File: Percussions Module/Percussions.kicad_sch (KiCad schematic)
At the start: 86 parts

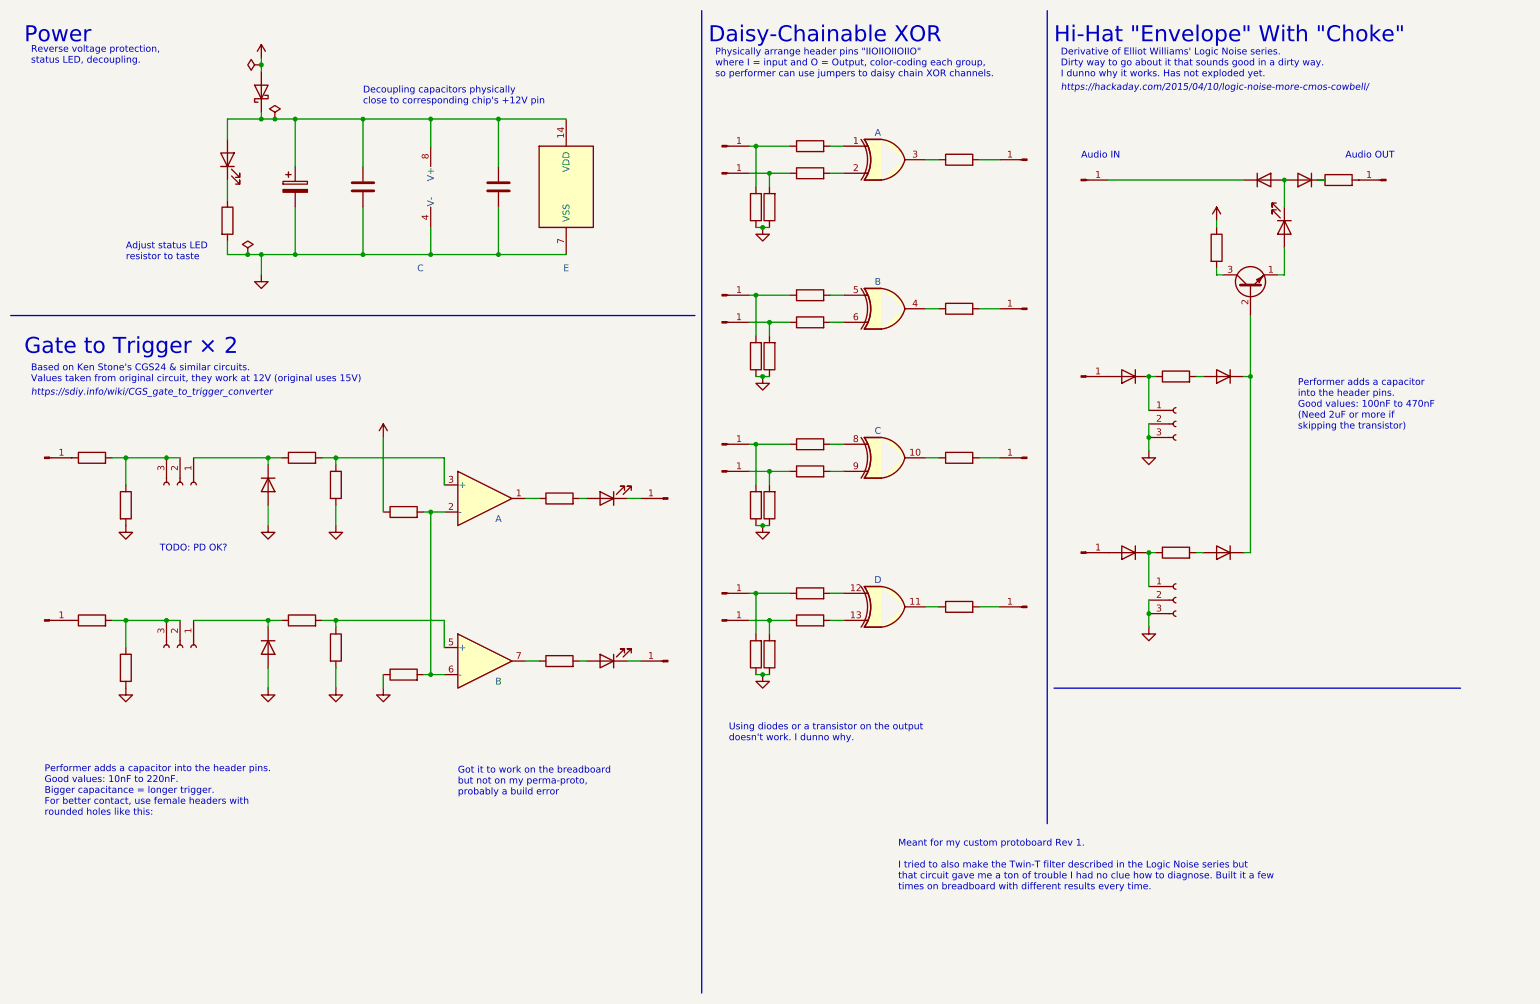
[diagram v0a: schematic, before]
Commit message: Try out switching sequencer
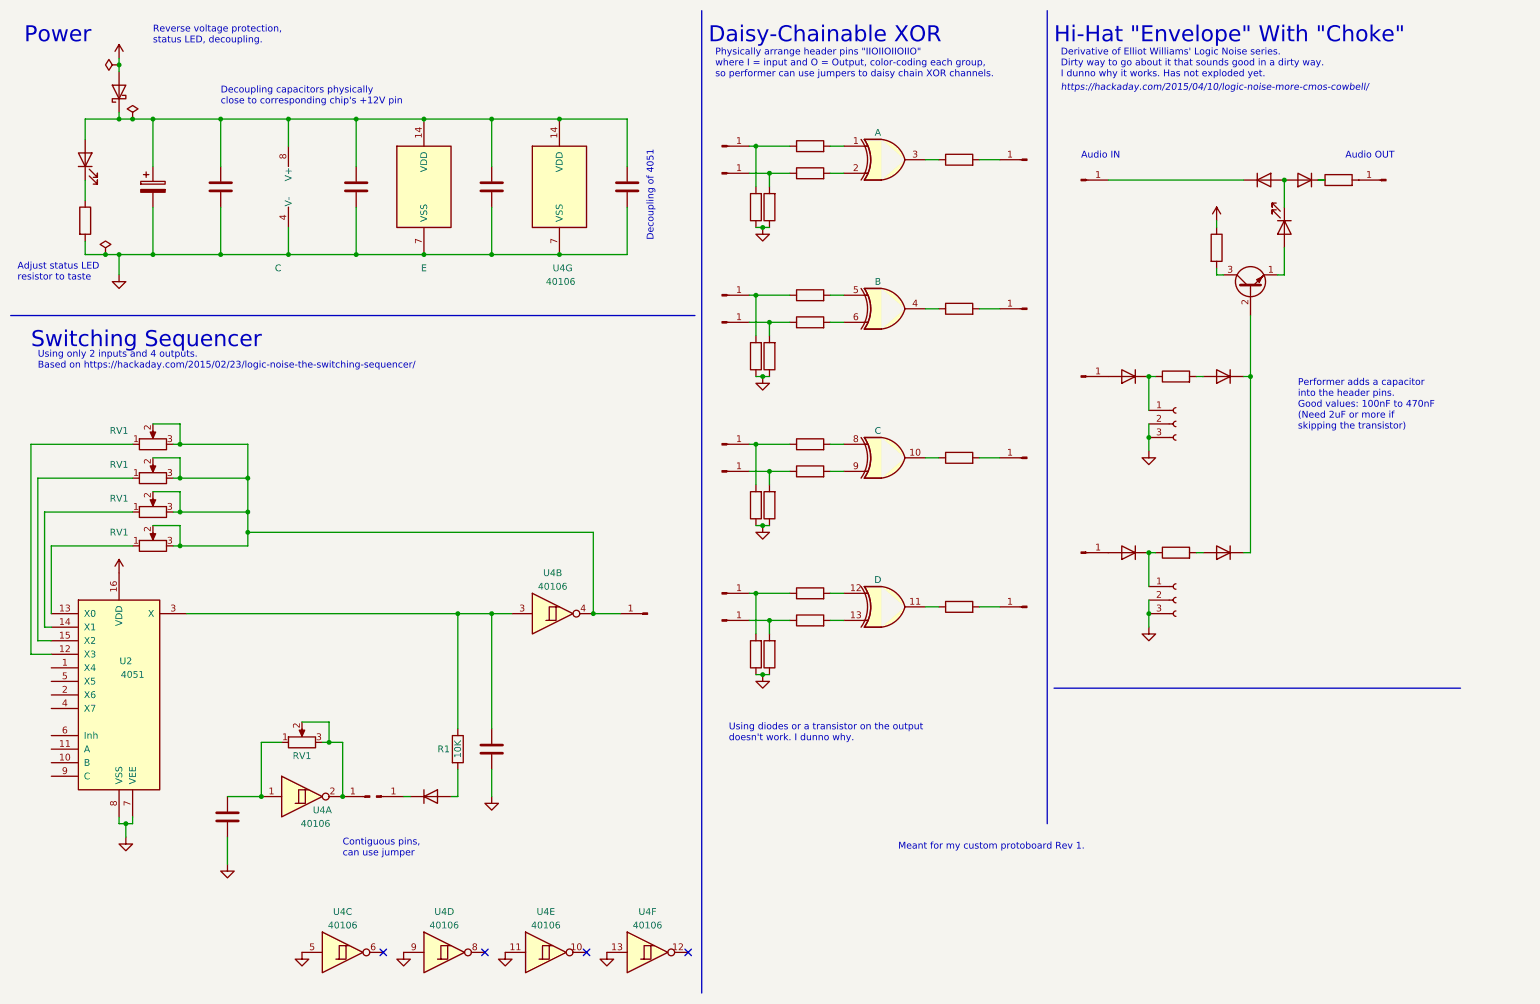
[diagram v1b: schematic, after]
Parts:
- removed ? (x4): (no value), symbol Connector:Conn_01x01_Male
- removed ? (x2): (no value), symbol Diode:1N4148
- removed ? (x12): (no value), symbol Device:R
- removed ? (x2): (no value), symbol Device:LED
- removed ? (x2): (no value), symbol Amplifier_Operational:LM358
- removed ? (x2): (no value), symbol Connector:Conn_01x03_Female
- added ? (x4): (no value), symbol Device:C
- added ?: (no value), symbol Diode:1N4148
- added ? (x3): (no value), symbol Connector:Conn_01x01_Male
- added R1: 10K, symbol Device:R
- added RV1 (x5): R_Potentiometer, symbol Device:R_Potentiometer
- added U2: 4051, symbol 4xxx:4051
- added U4: 40106, symbol 4xxx:40106
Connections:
- net +12V: now also U2.16 (VDD)
- net GND: now also ?.2, ?.2, ?.2, ?.2, U2.7 (VEE), U2.8 (VSS), U4.11, U4.13, U4.5, U4.7 (VSS), U4.9
- net at ?.1, ?.1, ?.1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: now also ?.1, ?.1, U4.14 (VDD)
- new net: RV1.1, U2.12 (X3)
- new net: RV1.1, U2.13 (X0)
- new net: RV1.1, U2.14 (X1)
- new net: RV1.1, U2.15 (X2)
- new net: ?.1, R1.1, U2.3 (X), U4.3
- new net: ?.1 (Pin_1), RV1.2, RV1.2, RV1.2, RV1.2, RV1.3, RV1.3, RV1.3, RV1.3, U4.4
- new net: ?.1 (K), ?.1 (Pin_1)
- new net: ?.2 (A), R1.2
- new net: ?.1, RV1.1, U4.1
- new net: ?.1 (Pin_1), RV1.2, RV1.3, U4.2
- no-connect marks 0 -> 4
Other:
- note added: "Contiguous pins, can use jumper"
- note added: "Decoupling of 4051"
- note added: "Meant for my custom protoboard Rev 1."
- note added: "Switching Sequencer"
- note added: "Using only 2 inputs and 4 outputs. Based on https://hackaday.com/2015/02/23/logic-noise-the-switching-sequencer/"
- note removed: "Based on Ken Stone's CGS24 & similar circuits. Values taken from original circuit, they work at 12V (original uses 15V)"
- note removed: "Gate to Trigger × 2"
- note removed: "Got it to work on the breadboard but not on my perma-proto, probably a build error"
- note removed: "Meant for my custom protoboard Rev 1. I tried to also make the Twin-T filter described in the Logic Noise series but that circuit gave me a ton of trouble I had no clue how to diagnose. Built it a few times on breadboard with different results every time."
- note removed: "Performer adds a capacitor into the header pins. Good values: 10nF to 220nF. Bigger capacitance = longer trigger. For better contact, use female headers with rounded holes like this:"
- note removed: "TODO: PD OK?"
- note removed: "https://sdiy.info/wiki/CGS_gate_to_trigger_converter"
- title: Percussions Board [WIP] -> Percussions & Switching Sequencer
- moved on the sheet: C, E

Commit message: Percussions add switching sequencer
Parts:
- added ? (x5): (no value), symbol Device:R
- added ? (x10): (no value), symbol Connector:Conn_01x01_Male
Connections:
- net GND: now also U2.6 (Inh), U2.9 (C), U4.1, U4.3, ?.1, ?.1; no longer U4.5, U4.9
- net at U4.8: now also ?.1, ?.1 (Pin_1), ?.1 (Pin_1), ?.1 (Pin_1), ?.1 (Pin_1)
- net at U2.10 (B): now also ?.2, ?.2
- net at U2.11 (A): now also ?.2, ?.2
- net at RV1.1, U2.12 (X3): now also RV1.2
- net at RV1.1, U2.13 (X0): now also RV1.2
- net at RV1.1, U2.14 (X1): now also RV1.2
- net at RV1.1, U2.15 (X2): now also RV1.2
- net at ?.1, R1.1, U2.3 (X): now also U4.9; no longer U4.3
- net at ?.1, RV1.1: now also RV1.2, U4.5; no longer U4.1
- net at ?.1 (Pin_1), RV1.3: now also U4.6; no longer RV1.2, U4.2
- new net: ?.1, ?.1 (Pin_1) (x2)
- new net: ?.1 (Pin_1), RV1.3 (x4)
- new net: ?.1 (Pin_1), ?.2
- now unconnected: U4.4
- no-connect marks 4 -> 8
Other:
- note added: "Can use any two pairs of inverters. Tie unused inputs to GND. Using other inputs for something else would generate a lot of crosstalk."
- note added: "Performer adds a capacitor into the header pins. Good values: 100nF to 470nF (Need 2uF or more if skipping the transistor) Use female header pins with rounded metal contacts."
- note added: "Test both 40106 capacitor values before committing, they influence pitch and depend on input voltage."
- note removed: "Performer adds a capacitor into the header pins. Good values: 100nF to 470nF (Need 2uF or more if skipping the transistor)"
- moved on the sheet: R1, RV1, U2, U4E, U4F
